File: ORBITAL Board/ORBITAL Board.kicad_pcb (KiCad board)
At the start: 4 copper layers, 73.2 x 30.5 mm, 53 parts, among them J1 Conn_01x02, J2 Micro_SD_Card_Det, J3 Conn_01x02, J4 Conn_01x12, J5 Conn_01x12, P1 USB_C_Plug_USB2.0, U1 W25Q128JVS, U2 RP2040, U3 MS5607-02BA, U5 BNO085, U8 USBLC6-2SC6

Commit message: Uploading Board Progress
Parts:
- added AE1: Antenna, GPS:SMA_Molex_73251-1153_EdgeMount_Horizontal, F.Cu at (74.5, 61.1)
- added AE2: Antenna, GPS:SMA_Molex_73251-1153_EdgeMount_Horizontal, F.Cu at (74.5, 74.4)
- added C1: 22n, Capacitor_SMD:C_0402_1005Metric, F.Cu at (202.4, 48.6)
- added C10: 47n, Capacitor_SMD:C_0402_1005Metric, F.Cu at (202.4, 56.5)
- added C11: 47n, Capacitor_SMD:C_0402_1005Metric, F.Cu at (202.4, 58.4)
- added C12: 10n, Capacitor_SMD:C_0402_1005Metric, F.Cu at (205.3, 48.6)
- added C13: .1u, Capacitor_SMD:C_0402_1005Metric, F.Cu at (205.3, 50.5)
- added C14: 100u, Capacitor_SMD:C_0402_1005Metric, F.Cu at (205.3, 52.5)
- added C15: .1u, Capacitor_SMD:C_0402_1005Metric, F.Cu at (205.3, 54.5)
- added C16: 22U, Capacitor_SMD:C_0402_1005Metric, F.Cu at (205.3, 56.5)
- added C19: 22p, Capacitor_SMD:C_0402_1005Metric_Pad0.74x0.62mm_HandSolder, F.Cu at (203.3, 37.0)
- added C2: 10u, Capacitor_SMD:C_0402_1005Metric, F.Cu at (210.3, 33.0)
- added C21: 22u, Capacitor_SMD:C_0402_1005Metric_Pad0.74x0.62mm_HandSolder, F.Cu at (203.3, 38.9)
- added C24: 100n, Capacitor_SMD:C_0402_1005Metric_Pad0.74x0.62mm_HandSolder, F.Cu at (203.2, 40.9)
- added C25: 10n, Capacitor_SMD:C_0402_1005Metric, F.Cu at (205.3, 58.4)
- added C27: 1n, Capacitor_SMD:C_0402_1005Metric, F.Cu at (208.1, 48.6)
- added C3: 100n, Capacitor_SMD:C_0402_1005Metric_Pad0.74x0.62mm_HandSolder, F.Cu at (203.3, 33.0)
- added C33: 2.2u, Capacitor_SMD:C_0402_1005Metric, F.Cu at (208.1, 50.5)
- added C35: 22u, Capacitor_SMD:C_0402_1005Metric, F.Cu at (208.1, 52.5)
- added C39: 100n, Capacitor_SMD:C_0402_1005Metric_Pad0.74x0.62mm_HandSolder, F.Cu at (203.3, 42.9)
- added C6: 22U, Capacitor_SMD:C_0402_1005Metric_Pad0.74x0.62mm_HandSolder, F.Cu at (203.3, 35.0)
- added C7: 4.7u, Capacitor_SMD:C_0402_1005Metric, F.Cu at (202.4, 50.5)
- added C8: 1.8n, Capacitor_SMD:C_0402_1005Metric, F.Cu at (202.4, 52.5)
- added C9: 10n, Capacitor_SMD:C_0402_1005Metric, F.Cu at (202.4, 54.5)
- added D1: D_Small, Diode_SMD:D_0603_1608Metric, F.Cu at (164.3, 40.6)
- added L1: 4.7u, Inductor_SMD:L_0603_1608Metric, F.Cu at (206.9, 33.3)
- added L2: 3.3u, Inductor_SMD:L_0603_1608Metric, F.Cu at (190.9, 48.8)
- added L3: 39n, Inductor_SMD:L_0603_1608Metric, F.Cu at (79.7, 55.8)
- added L4: 39n, Inductor_SMD:L_0603_1608Metric, F.Cu at (79.7, 58.3)
- added R1: 500K, Resistor_SMD:R_0603_1608Metric, F.Cu at (190.9, 51.4)
- added R10: 40.2K, Resistor_SMD:R_0603_1608Metric, F.Cu at (190.9, 61.4)
- added R11: 225k, Resistor_SMD:R_0603_1608Metric, F.Cu at (206.9, 35.8)
- added R12: 4.7K, Resistor_SMD:R_0603_1608Metric, F.Cu at (194.9, 48.8)
- added R13: 4.7K, Resistor_SMD:R_0603_1608Metric, F.Cu at (194.9, 51.4)
- added R14: 4.7K, Resistor_SMD:R_0603_1608Metric, F.Cu at (194.9, 53.9)
- added R16: 100K, Resistor_SMD:R_0603_1608Metric, F.Cu at (206.9, 38.3)
- added R17: 50k, Resistor_SMD:R_0603_1608Metric, F.Cu at (206.9, 40.8)
- added R18: 18, Resistor_SMD:R_0603_1608Metric, F.Cu at (194.9, 56.4)
- added R19: 18, Resistor_SMD:R_0603_1608Metric, F.Cu at (194.9, 58.9)
- added R2: 100K, Resistor_SMD:R_0603_1608Metric, F.Cu at (190.9, 53.9)
- added R20: 1K, Resistor_SMD:R_0603_1608Metric, F.Cu at (194.9, 61.4)
- added R21: 47K, Resistor_SMD:R_0603_1608Metric, F.Cu at (198.9, 48.8)
- added R24: .33, Resistor_SMD:R_0603_1608Metric, F.Cu at (198.9, 51.4)
- added R25: .33, Resistor_SMD:R_0603_1608Metric, F.Cu at (198.9, 53.9)
- added R3: 350K, Resistor_SMD:R_0603_1608Metric, F.Cu at (190.9, 56.4)
- added R4: 510K, Resistor_SMD:R_0603_1608Metric, F.Cu at (190.9, 58.9)
- added RB1: 100K, Resistor_SMD:R_0603_1608Metric, F.Cu at (198.9, 56.4)
- added RB2: 100K, Resistor_SMD:R_0603_1608Metric, F.Cu at (198.9, 58.9)
- added U1: PTPS563206DRLR, footprints:SOT_07SDRLR_TEX, F.Cu at (100.8, 37.6)
- added U6: STSPIN220, Package_DFN_QFN:VQFN-16-1EP_3x3mm_P0.5mm_EP1.8x1.8mm, F.Cu at (140.8, 69.3)
- added U7: ~, GPS:PX1172RH, F.Cu at (79.6, 96.5)
- moved J1 10.2 mm to (149.9, 55.9)
- moved U5 9.15 mm to (116.6, 68.4)
- moved P1 8.06 mm to (155.7, 63.2)
- moved C36 7.93 mm to (165.1, 48.3)
- moved J1 7.66 mm to (160.0, 70.5)
- moved U2 6.43 mm to (145.8, 42.5)
- moved U8 4.00 mm to (110.3, 45.7)
- renumbered C2 to C17, C8 to C18, C22 to C20, C23 to C22, C3 to C23, C9 to C28, C4 to C29, C10 to C30, C5 to C31, C6 to C32, C7 to C34, C11 to C36, C12 to C37, C13 to C38, C19 to C4, C1 to C5, J3 to J1, J5 to J3, R5 to R15, R1 to R22, R2 to R23, R8 to R26, R7 to R27, R6 to R28, R14 to R5, R3 to R6, R4 to R7, R18 to R8, R19 to R9, U1 to U2, U8 to U3, U3 to U8
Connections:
- C17 pad 2: Net-(C2-Pad2) -> Net-(U5-XIN)
- C18 pad 2: Net-(C8-Pad2) -> Net-(C18-Pad2)
- R15 pad 1: Net-(C8-Pad2) -> Net-(C18-Pad2)
- R15 pad 2: Net-(R5-Pad2) -> Net-(U5-XOUT)
- R22 pad 1: Net-(R1-Pad1) -> Net-(U5-USB_DP)
- R23 pad 2: Net-(R2-Pad2) -> Net-(U5-USB_DM)
- R27 pad 2: /SDA -> /D0
- R28 pad 1: /SCL -> /D1
- U8 pad 7: /SDA -> /D0
- U8 pad 8: /SCL -> /D1

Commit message: Adding schematic and PCB updates
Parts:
- added BT1: MS920SE, BackupBattery:BAT_MS920SE-FL27E, F.Cu at (199.7, 95.8)
- added C41: 22u, Capacitor_SMD:C_0603_1608Metric, F.Cu at (101.0, 51.5)
- added C6: 22u, Capacitor_SMD:C_0603_1608Metric, F.Cu at (101.0, 49.0)
- added Y1: ABLS-12.000MHZ-B4-T, Crystal:Crystal_SMD_Abracon_ABM8G-4Pin_3.2x2.5mm, F.Cu at (128.4, 69.4)
- C13, C15: value .1u -> 100n
- D1: footprint Diode_SMD:D_0603_1608Metric -> GPS:DIO_RB400DFH_ROM-M
- R12, R13, R14: value 4.7K -> 5.1K
- moved J2 94.5 mm to (172.7, 127.7)
- moved AE1 89.0 mm to (104.8, 144.8)
- moved U2 76.6 mm to (172.7, 114.3)
- moved J1 68.3 mm to (175.2, 137.2)
- moved J3 67.3 mm to (127.0, 147.3)
- moved U2 57.0 mm to (140.4, 124.5)
- moved J4 47.5 mm to (154.9, 101.6)
- moved AE2 44.3 mm to (104.8, 106.7)
- moved U7 32.6 mm to (102.8, 119.4)
- moved P1 19.5 mm to (160.0, 82.2)
- moved U8 18.3 mm to (125.9, 55.3)
- moved J1 11.4 mm to (139.7, 50.8)
- moved U5 10.8 mm to (105.8, 68.3)
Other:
- board size 73.2 x 30.5 mm -> 80 x 96.7 mm

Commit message: Updating board + adding in board notes
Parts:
- removed the J1 at (139.7, 50.8)
- BT1, P1, U1: moved to B.Cu
- moved P1 46.9 mm to (115.3, 96.2)
- moved U8 28.9 mm to (133.5, 83.2)
- moved BT1 28.9 mm to (173.7, 108.5), turned to 180 degrees
- moved U2 2.18 mm to (173.8, 116.2)
- turned U1 to 180 degrees

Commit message: Updating PCB Layout
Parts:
- added R29: 9000, Resistor_SMD:R_0603_1608Metric, F.Cu at (179.5, 55.9)
- added R30: 2000, Resistor_SMD:R_0603_1608Metric, F.Cu at (179.5, 60.9)
- BT1, J1, P1, U1: moved to F.Cu
- D1: value D_Small -> D_Zener
- moved J2 117.6 mm to (55.4, 120.8)
- moved U2 117.5 mm to (57.4, 132.1)
- moved U3 102.7 mm to (97.7, 143.2)
- moved BT1 84.3 mm to (91.2, 125.7), turned to 0 degrees
- moved U8 76.4 mm to (59.9, 103.5)
- moved AE2 74.5 mm to (51.5, 158.6), turned to 56.25 degrees
- moved U1 74.1 mm to (108.4, 111.3), turned to 0 degrees
- moved J3 70.6 mm to (89.2, 87.7), turned to -90 degrees
- moved U2 68.9 mm to (74.4, 105.0), turned to 0 degrees
- moved J4 68.4 mm to (89.2, 82.7)
- moved J1 57.8 mm to (119.4, 121.9), turned to 90 degrees
- moved U5 54.8 mm to (142.2, 109.2)
- moved P1 54.1 mm to (104.6, 149.3)
- moved U7 50.1 mm to (63.1, 149.9)
- moved AE1 17.4 mm to (96.5, 160.0), turned to 123.75 degrees
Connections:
- C25 pad 1: /D6 -> Net-(U6-EN/FLT)
- C27 pad 1: /D7 -> Net-(U6-STBY/RESET)
- J2 pad 1: /SD_DAT2 -> unconnected-(J2-DAT2-Pad1)
- J2 pad 2: /SD_DAT3 -> /SD_CS
- J2 pad 3: /SD_CMD -> /SD_DIN
- J2 pad 5: /CLK_OUT -> /SD_SCLK
- J2 pad 7: /SD_DAT0 -> /SD_DOUT
- J2 pad 8: /SD_DAT1 -> unconnected-(J2-DAT1-Pad8)
- R18 pad 1: /D6 -> Net-(U6-EN/FLT)
- R19 pad 1: /D7 -> Net-(U6-STBY/RESET)
- U6 pad 11: /A3 -> /VRef
- U6 pad 13: /D6 -> Net-(U6-EN/FLT)
- U6 pad 14: /D7 -> Net-(U6-STBY/RESET)
- U6 pad 15: unconnected-(U6-MODE2-Pad15) -> /D3
- U6 pad 16: unconnected-(U6-MODE1-Pad16) -> /D2
- U7 pad 37: unconnected-(U7-GND-Pad37) -> GND
- U7 pad 41: unconnected-(U7-GND-Pad41) -> GND
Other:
- board size 80 x 96.7 mm -> 137.1 x 118.7 mm

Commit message: Updating PCB
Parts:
- moved D1 137.3 mm to (86.4, 153.6)
- moved U6 108.5 mm to (39.2, 107.4)
- moved U5 93.4 mm to (49.1, 101.3)
- moved Y1 50.7 mm to (90.0, 102.5)
- moved BT1 27.0 mm to (105.9, 148.3), turned to 90 degrees
- moved AE1 21.9 mm to (75.4, 165.7), turned to 90 degrees
- moved AE2 21.9 mm to (37.8, 141.7), turned to 22.5 degrees
- moved P1 14.3 mm to (110.6, 136.3)
- moved U7 13.3 mm to (50.8, 144.8)
- moved U1 11.8 mm to (98.3, 117.3)
- moved U3 10.2 mm to (87.5, 143.2)
- moved J1 3.72 mm to (118.3, 118.3)
- moved U2 2.63 mm to (73.7, 102.5)
- moved U8 2.54 mm to (59.9, 100.9)
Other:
- board size 137.1 x 118.7 mm -> 94 x 94 mm

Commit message: Updating ORBITAL PCB
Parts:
- removed the C20 at (176.6, 43.0)
- BT1: footprint BackupBattery:BAT_MS920SE-FL27E -> GPS:BT1
- D1: footprint GPS:DIO_RB400DFH_ROM-M -> GPS:DFLS130L
- U5: renamed from U2; footprint Custom footprints:RP2040-QFN-56 -> RP2040:RP2040-QFN-56
- moved C4 184.4 mm to (40.5, 136.1), turned to 180 degrees
- moved R5 167.7 mm to (49.1, 136.3), turned to 180 degrees
- moved C30 135.0 mm to (83.7, 96.1)
- moved C20 134.6 mm to (68.9, 93.2), turned to 180 degrees
- moved R15 133.8 mm to (60.2, 95.5), turned to -90 degrees
- moved C17 130.0 mm to (66.5, 101.4)
- moved C37 128.2 mm to (83.7, 94.8)
- moved C23 127.0 mm to (68.7, 96.8), turned to 180 degrees
- moved C18 125.2 mm to (60.4, 90.7), turned to 180 degrees
- moved C38 121.7 mm to (78.9, 86.8), turned to 180 degrees
- moved C22 118.4 mm to (68.9, 94.9), turned to 180 degrees
- moved R23 118.3 mm to (98.8, 110.8), turned to -177.5 degrees
- moved C34 115.5 mm to (83.7, 92.0)
- moved R27 115.0 mm to (78.8, 96.6), turned to -179.6 degrees
- moved C28 113.9 mm to (83.7, 93.3)
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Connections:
- BT1 pad N: (no net) -> GND
- BT1 pad P: (no net) -> /V_BCK
- U5 pad 18: /SD_CMD -> unconnected-(U5-GPIO15-Pad18)
- U5 pad 20: Net-(C2-Pad2) -> Net-(U5-XIN)
- U5 pad 21: Net-(R5-Pad2) -> Net-(U5-XOUT)
- U5 pad 27: /SD_DAT0 -> /SD_DOUT
- U5 pad 28: /SD_DAT1 -> /SD_CS
- U5 pad 29: /SD_DAT2 -> /SD_SCLK
- U5 pad 30: /SD_DAT3 -> /SD_DIN
- U5 pad 35: /CLK_OUT -> unconnected-(U5-GPIO23-Pad35)
- U5 pad 36: /SDA -> unconnected-(U5-GPIO24-Pad36)
- U5 pad 37: /SCL -> unconnected-(U5-GPIO25-Pad37)
- U5 pad 46: Net-(R2-Pad2) -> Net-(U5-USB_DM)
- U5 pad 47: Net-(R1-Pad1) -> Net-(U5-USB_DP)
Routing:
- net GND: track 0.00 -> 135.9 mm, vias 0 -> 4
- net +3.3V: track 0.00 -> 80.5 mm, vias 0 -> 6
- net Net-(AE1-A): track 0.00 -> 32.3 mm
- net /D0: track 0.00 -> 30.4 mm
- net Net-(U5-USB_DP): track 0.00 -> 27.5 mm
- net /D1: track 0.00 -> 27.0 mm
- net /V_BCK: track 0.00 -> 26.6 mm
- net +1V1: track 0.00 -> 25.9 mm, vias 0 -> 2
- net Net-(U5-USB_DM): track 0.00 -> 24.0 mm
- net /D2: track 0.00 -> 22.5 mm
- net /D11: track 0.00 -> 21.2 mm
- net /D8: track 0.00 -> 20.8 mm, vias 0 -> 1
- net /D3: track 0.00 -> 20.4 mm
- net /D10: track 0.00 -> 20.3 mm
- net Net-(AE2-A): track 0.00 -> 20.2 mm
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
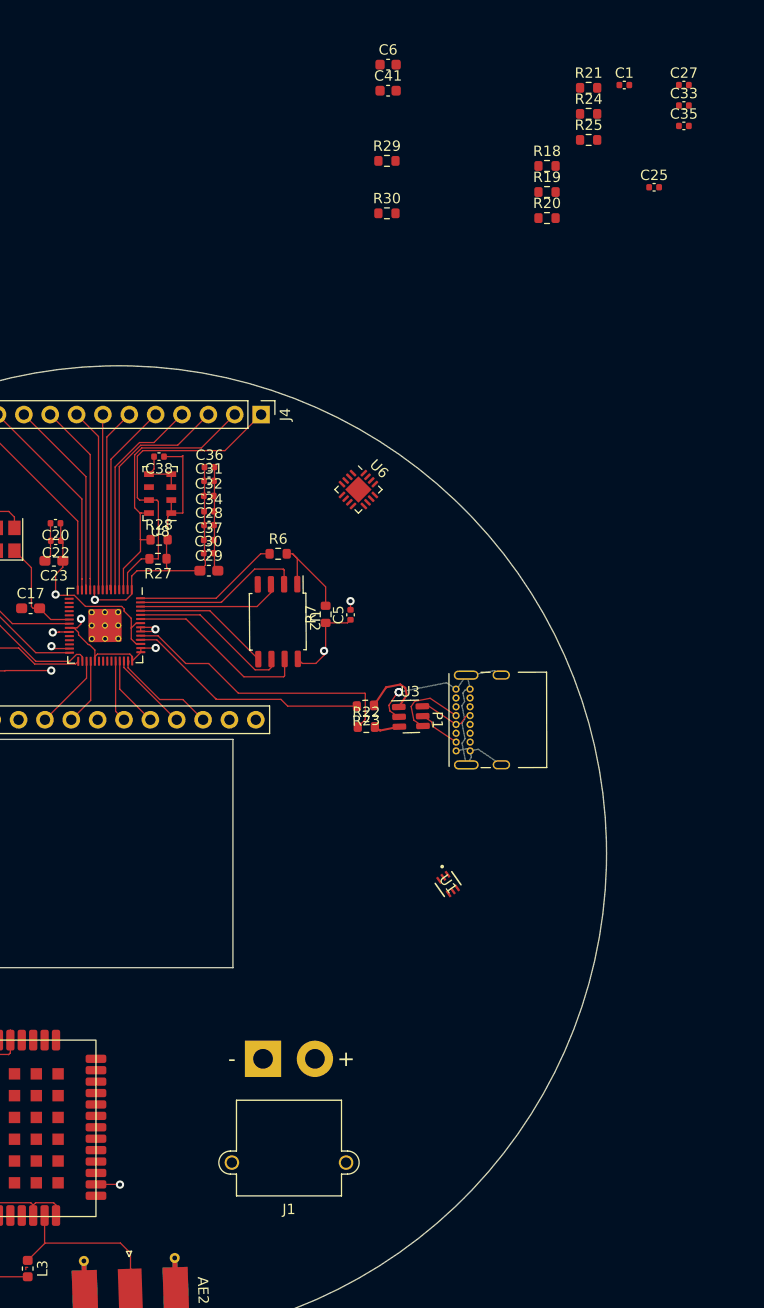
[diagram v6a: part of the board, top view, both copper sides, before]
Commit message: Implementing Motor Controller into PCB
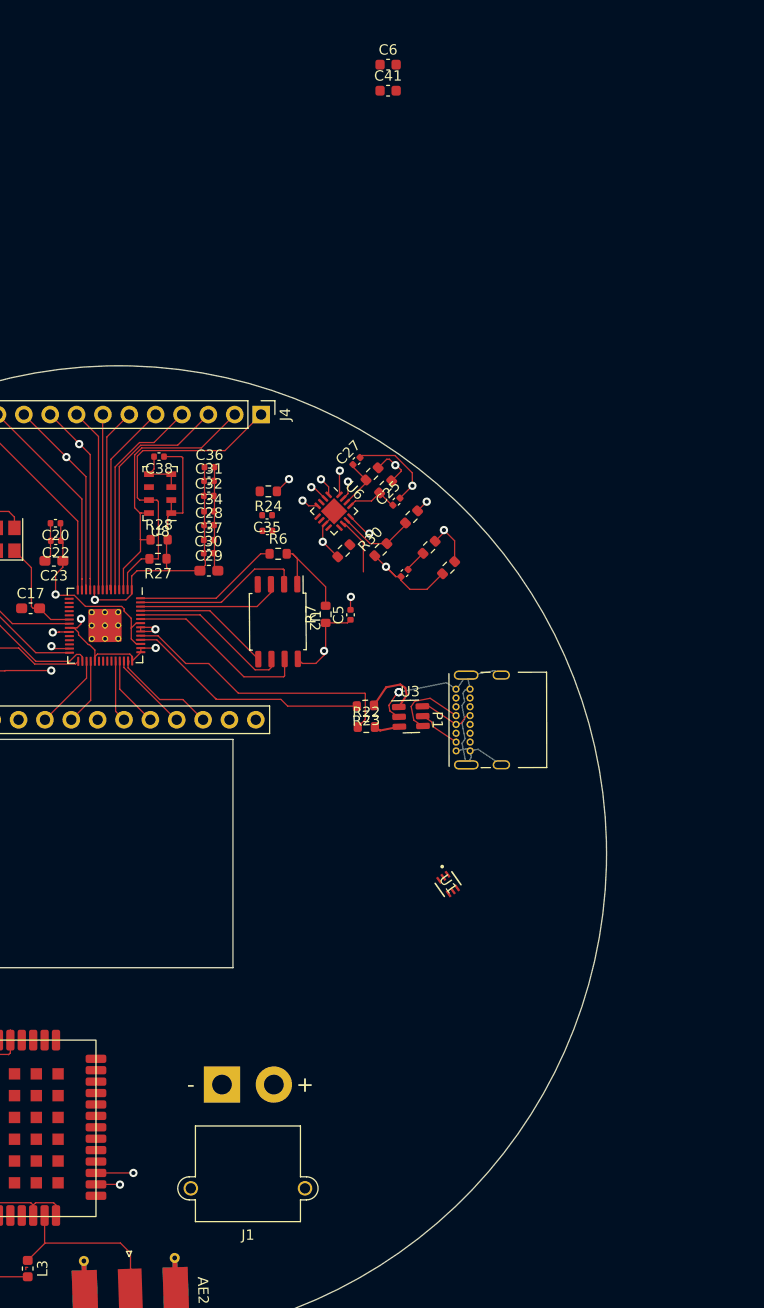
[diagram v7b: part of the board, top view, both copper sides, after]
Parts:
- moved C33 57.4 mm to (89.3, 93.9), turned to 180 degrees
- moved C35 55.0 mm to (89.3, 92.4), turned to 180 degrees
- moved C1 51.6 mm to (102.5, 98.0), turned to -135 degrees
- moved R21 48.2 mm to (106.8, 97.5), turned to -135 degrees
- moved C27 48.0 mm to (97.9, 87.2), turned to 45 degrees
- moved R24 47.7 mm to (89.4, 90.1), turned to 180 degrees
- moved R25 46.1 mm to (96.7, 95.8), turned to -135 degrees
- moved C25 39.2 mm to (101.8, 91.1), turned to 45 degrees
- moved R18 34.6 mm to (100.7, 89.7), turned to 45 degrees
- moved R29 34.4 mm to (103.2, 92.6), turned to 45 degrees
- moved R20 33.7 mm to (104.9, 95.5), turned to -135 degrees
- moved R30 32.4 mm to (100.3, 95.7), turned to 45 degrees
- moved R19 32.0 mm to (99.4, 88.4), turned to 45 degrees
- moved J1 4.67 mm to (84.9, 147.3)
- moved U6 3.14 mm to (95.7, 92.0)
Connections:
- BT1 pad N: GND -> (no net)
- BT1 pad P: /V_BCK -> (no net)
- J1 pad 1: +BATT -> GND
- J1 pad 2: GND -> +BATT
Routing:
- net /D8: track 20.8 -> 119.3 mm, vias 1 -> 2
- net /D9: track 19.5 -> 109.3 mm, vias 0 -> 2
- net GND: track 135.9 -> 160.6 mm, vias 4 -> 7
- net /D5: track 17.8 -> 40.1 mm, vias 0 -> 1
- net /D4: track 19.1 -> 39.7 mm, vias 0 -> 1
- net /D3: track 20.4 -> 40.9 mm, vias 0 -> 1
- net /D2: track 22.5 -> 42.8 mm, vias 0 -> 1
- net Net-(U6-TOFF): track 0.00 -> 16.7 mm, vias 0 -> 2
- net /VRef: track 0.00 -> 7.52 mm
- net Net-(U6-SENSEA): track 0.00 -> 5.97 mm, vias 0 -> 2
- net unconnected-(U6-OUTB1-Pad10): track 0.00 -> 5.53 mm
- net Net-(U6-EN/FLT): track 0.00 -> 5.10 mm
- net Net-(U6-STBY/RESET): track 0.00 -> 4.90 mm
- net +3.3V: track 80.5 -> 84.7 mm, vias 6 -> 7
- net Net-(C1-Pad1): track 0.00 -> 2.16 mm
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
